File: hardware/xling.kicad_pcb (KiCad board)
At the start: 2 copper layers, 35 x 47 mm, 55 parts, among them J1 ISP, J2 USB_OTG, J3 Battery, Q1 NTR0202PL, SW1 BTN, SW2 BTN, SW3 BTN, U1 REX012864L, U2 ATMEGA328P-AU, U3 MCP73831, U4 AP3401_TSOT26, Y1 12MHz

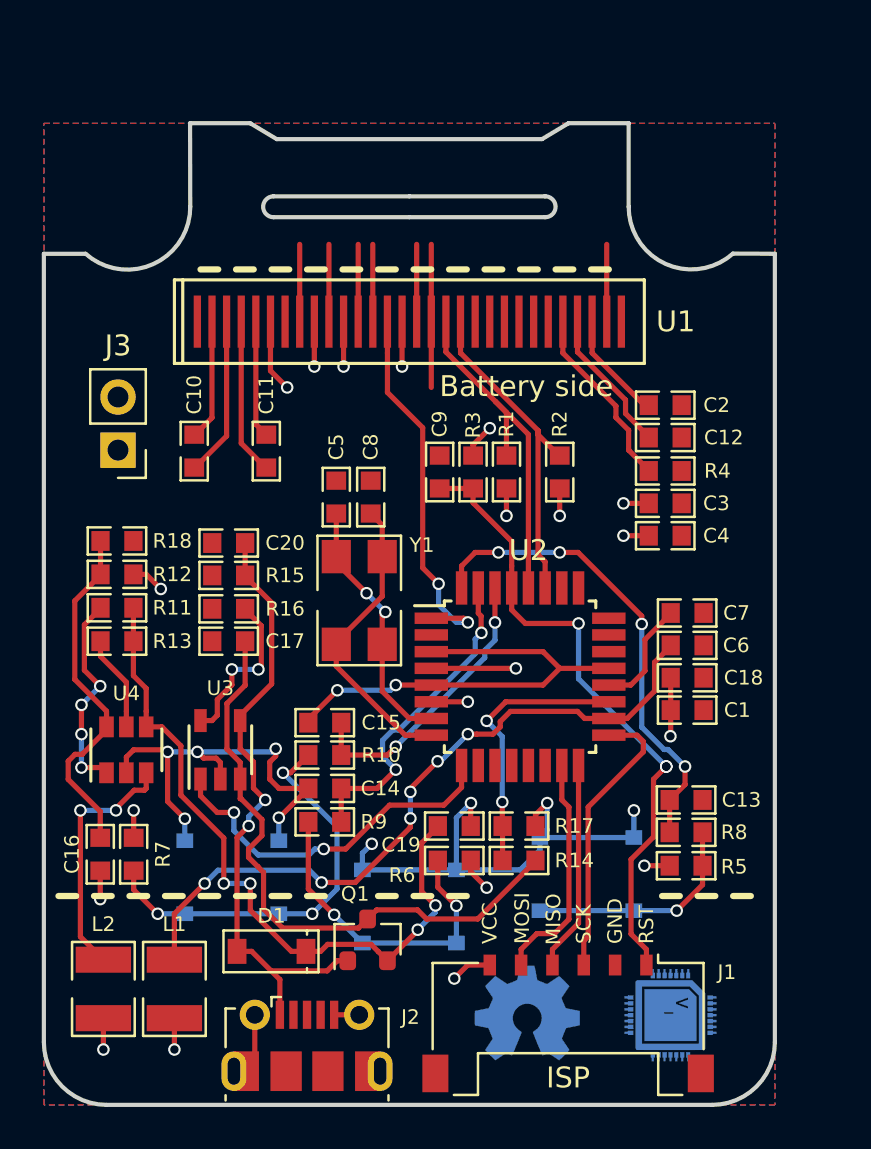
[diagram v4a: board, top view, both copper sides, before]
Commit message: patch 0.2.9: New battery SMD footprint.
ticket: N/A
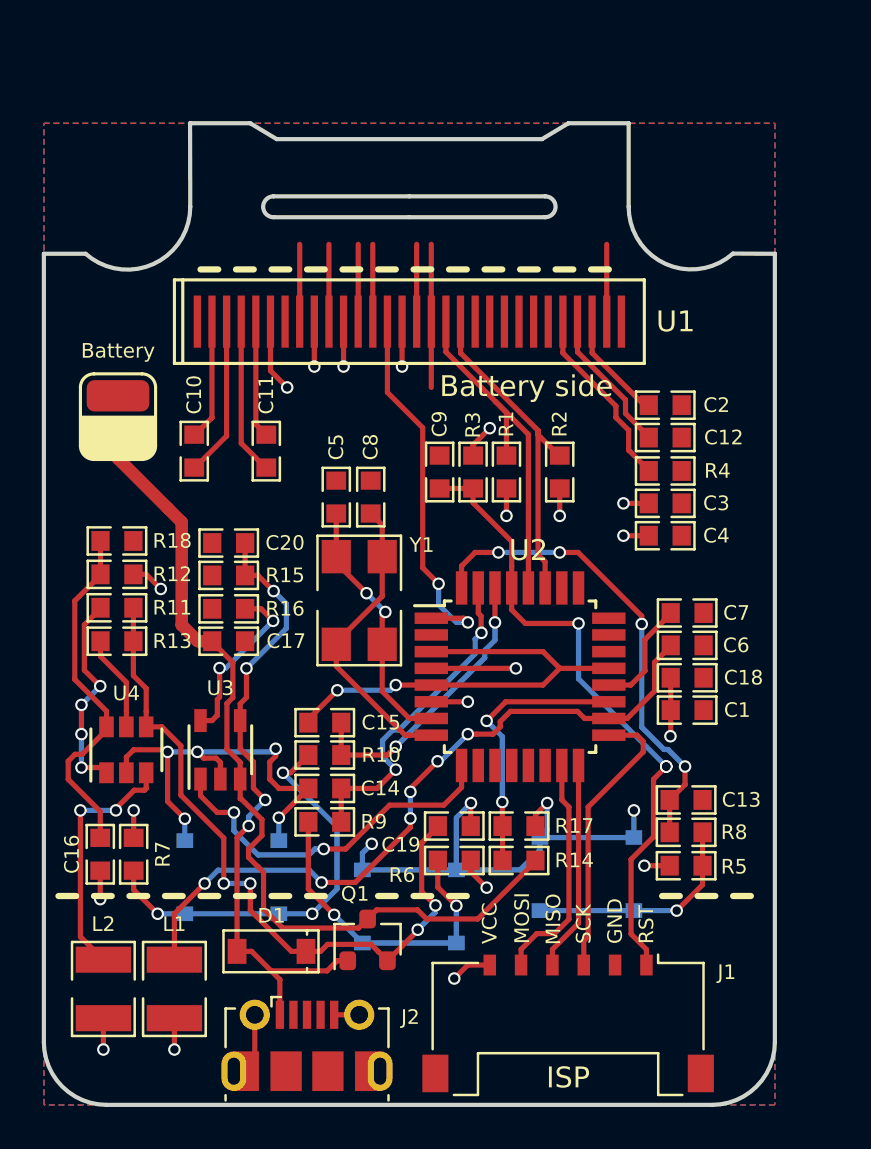
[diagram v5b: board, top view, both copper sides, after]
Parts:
- removed G***: LOGO, Xling Footprints:oshw
- removed G***: LOGO, Xling Footprints:mcusim
- J3: footprint Xling Footprints:PinHeader_1x02_P2.54mm_Vertical -> Xling Footprints:Battery_SMD_pads_1x02_HandSoldering
- moved J3 1.60 mm to (123.5, 94.0), turned to 90 degrees
- turned C17 to 0 degrees
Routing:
- net Net-(C17-Pad1): track 29.6 -> 41.8 mm
- net Net-(C20-Pad1): track 30.1 -> 31.3 mm, vias 2 -> 4
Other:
- board text added: "0.2.9 3.3V 128x64 1.28""
- board text added: "Battery"
- board text removed: "0.2.8 3.3V 128x64 1.28""

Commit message: patch 0.2.10: Add gaps to mount PCB correctly.
ticket: N/A
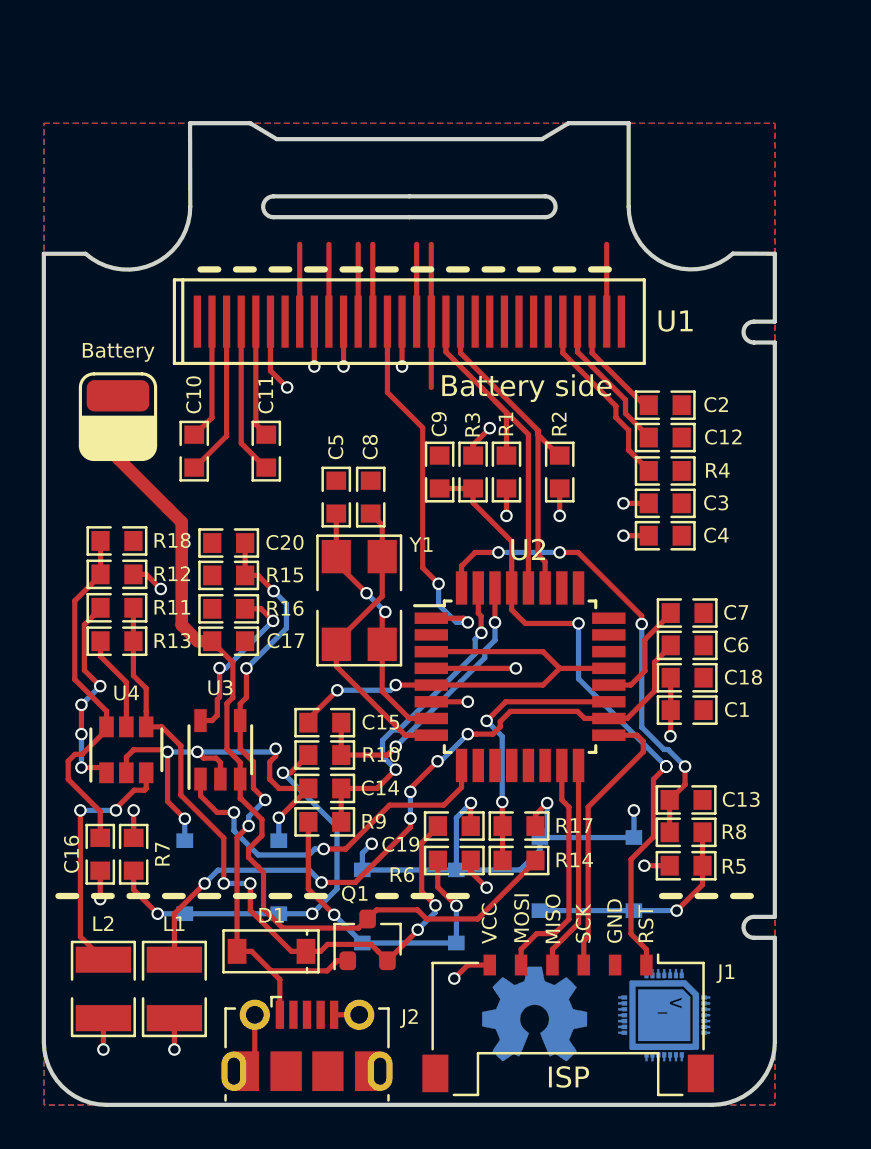
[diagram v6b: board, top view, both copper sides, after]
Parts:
- added G***: LOGO, Xling Footprints:mcusim, B.Cu at (149.7, 122.7)
- added G***: LOGO, Xling Footprints:oshw, B.Cu at (143.5, 122.7)
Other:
- outline, holes or cut-outs redrawn
- board text added: "0.2.10 3.3V 128x64 1.28""
- board text removed: "0.2.9 3.3V 128x64 1.28""

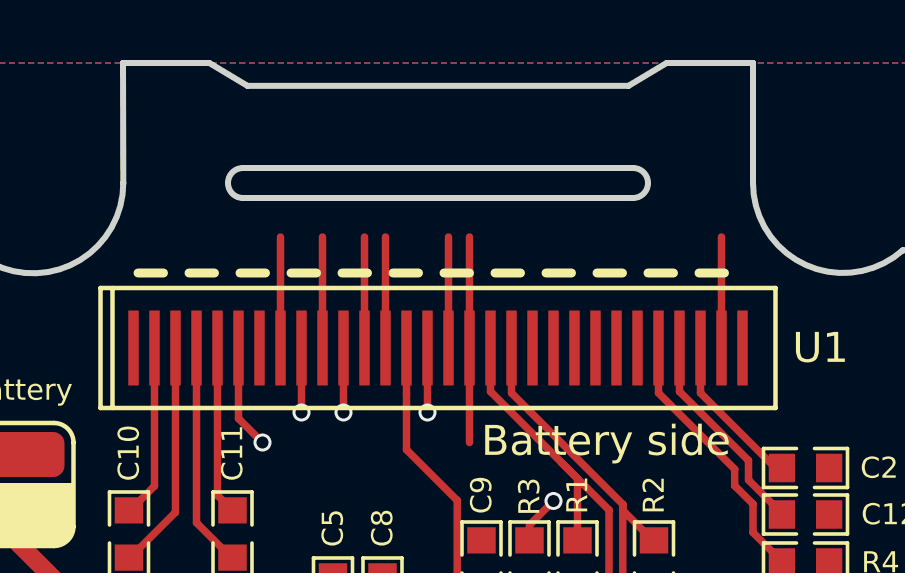
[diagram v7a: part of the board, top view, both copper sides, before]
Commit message: patch 0.2.12: Make a gap for OLED FFC bigger.
ticket: N/A

There is also a 3D package for Molex PicoFlex connector for AVR ISP.
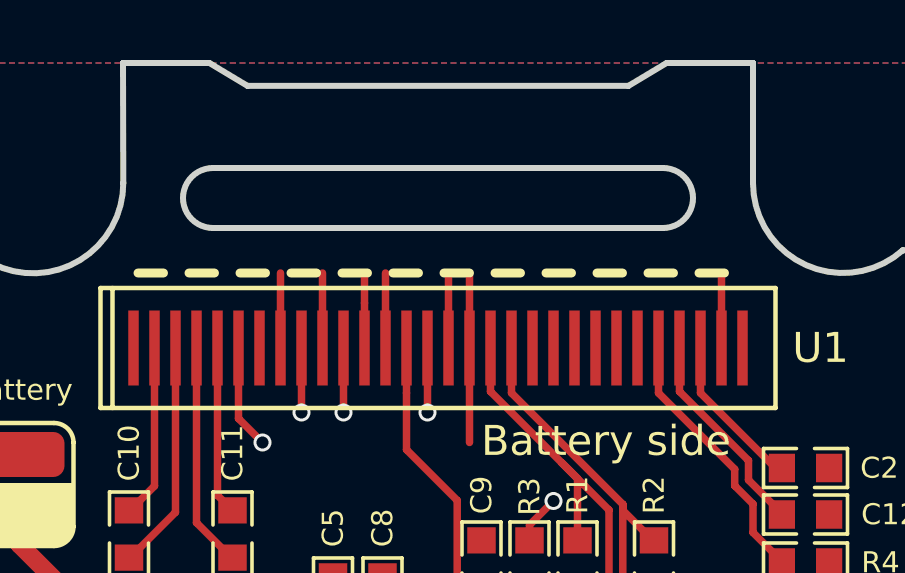
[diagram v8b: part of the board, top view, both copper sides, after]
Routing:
- net GND: track 101.2 -> 93.3 mm
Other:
- outline, holes or cut-outs redrawn
